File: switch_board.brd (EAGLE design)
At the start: 15 parts, among them U1 ADG904BRUZ, U2 ADP3330ARTZ-2.5-R7

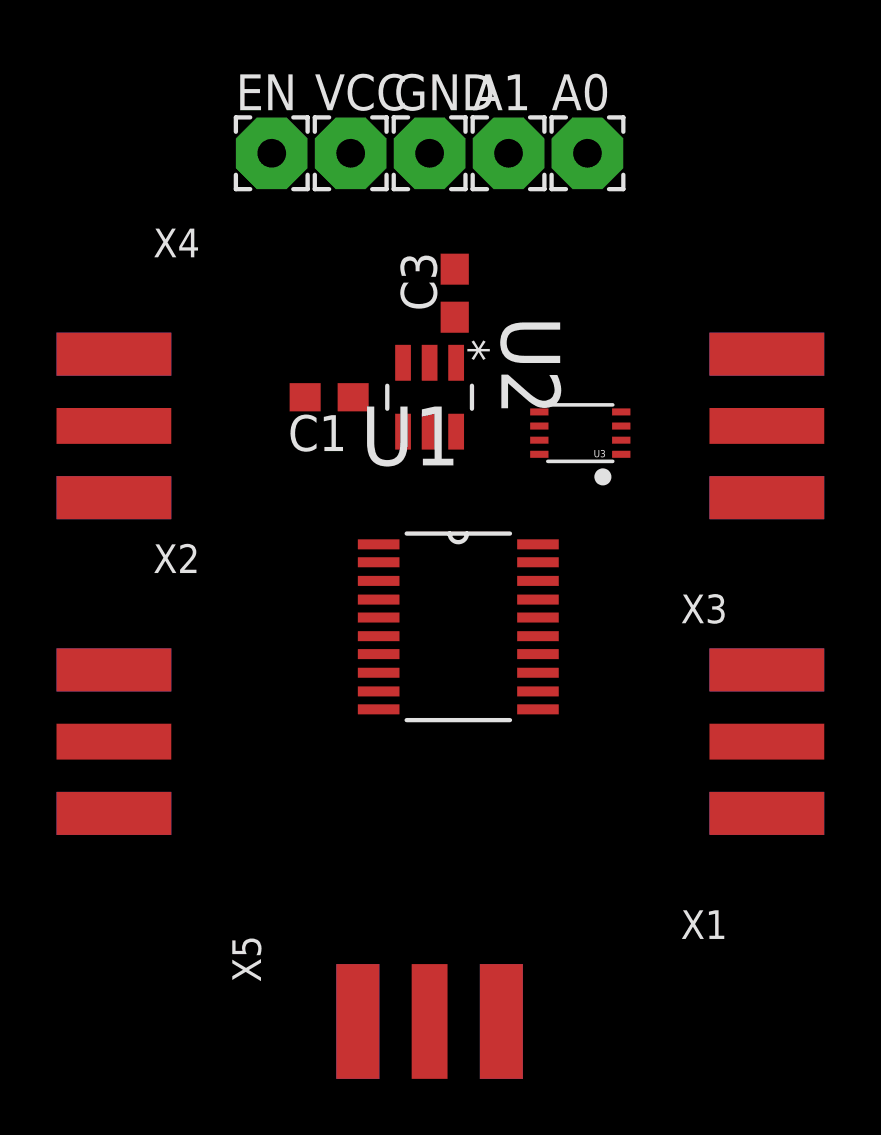
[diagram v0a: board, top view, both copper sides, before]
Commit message: Add DC Blocking Caps
Added 100uf caps for dc blocking on rf lines. Also updated readme
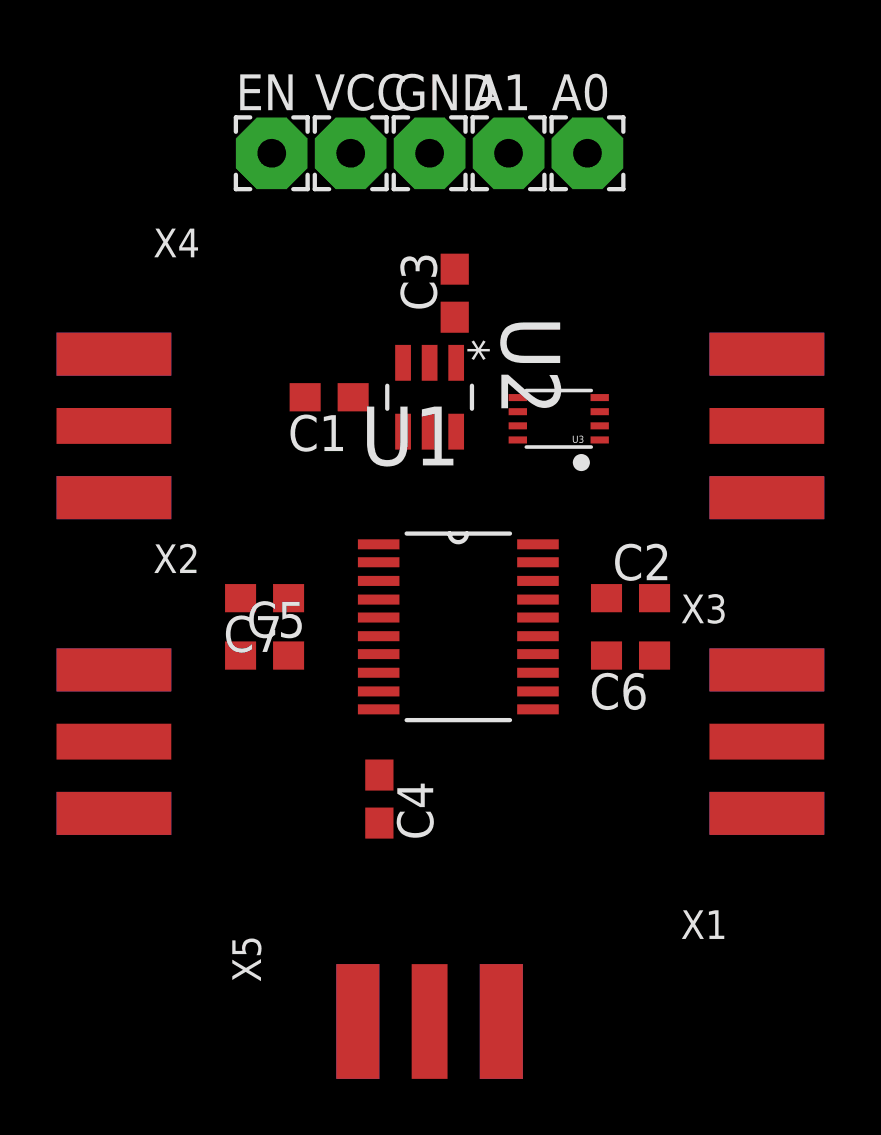
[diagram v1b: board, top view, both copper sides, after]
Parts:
- added C2, C4, C5, C6, C7: 0.1uF, resistor:C0603
- moved U3 0.92 mm to (17.8, 13.7)
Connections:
- removed net RF2: U1.17, X3.P
- new net N$3: C5.1, X2.P
- new net N$4: C4.1, U1.10
- new net N$5: C2.1, U1.17
- new net N$7: C2.2, X3.P
- new net N$8: C7.2, X4.P
- new net N$9: C6.1, X1.P
- net RF1: now also C7.1; no longer X4.P
- net RF3: now also C5.2; no longer X2.P
- net RF4: now also C6.2; no longer X1.P
- net RFC: now also C4.2; no longer U1.10
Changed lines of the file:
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@@
 <setting verticaltext="up"/>
 </settings>
-<grid distance="10" unitdist="mil" unit="mil" style="lines" multiple="1" display="no" altdistance="5" altunitdist="mil" altunit="mil"/>
+<grid distance="10" unitdist="mil" unit="mm" style="lines" multiple="1" display="yes" altdistance="5" altunitdist="mil" altunit="mil"/>
 <layers>
 <layer number="1" name="Top" color="4" fill="1" visible="yes" active="yes"/>
@@
 <element name="C1" library="resistor" library_urn="urn:adsk.eagle:library:348" package="C0603" value="0.47uF" x="9.652" y="14.478" rot="R180"/>
 <element name="C3" library="resistor" library_urn="urn:adsk.eagle:library:348" package="C0603" value="0.47uF" x="14.097" y="18.161" rot="R90"/>
-<element name="U3" library="adafruit" library_urn="urn:adsk.eagle:library:420" package="VFSOP-8" value="" x="18.542" y="13.208" rot="R90"/>
+<element name="U3" library="adafruit" library_urn="urn:adsk.eagle:library:420" package="VFSOP-8" value="" x="17.78" y="13.716" rot="R90"/>
+<element name="C2" library="resistor" library_urn="urn:adsk.eagle:library:348" package="C0603" value="0.1uF" x="20.32" y="7.366"/>
+<element name="C4" library="resistor" library_urn="urn:adsk.eagle:library:348" package="C0603" value="0.1uF" x="11.43" y="0.254" rot="R270"/>
+<element name="C5" library="resistor" library_urn="urn:adsk.eagle:library:348" package="C0603" value="0.1uF" x="7.366" y="5.334"/>
+<element name="C6" library="resistor" library_urn="urn:adsk.eagle:library:348" package="C0603" value="0.1uF" x="20.32" y="5.334" rot="R180"/>
+<element name="C7" library="resistor" library_urn="urn:adsk.eagle:library:348" package="C0603" value="0.1uF" x="7.366" y="7.366" rot="R180"/>
 </elements>
 <signals>
@@
 <contactref element="X4" pad="GND@4"/>
 <contactref element="X4" pad="GND@3"/>
-<contactref element="X3" pad="GND@4"/>
-<contactref element="X3" pad="GND@3"/>
 <contactref element="X3" pad="GND@2"/>
 <contactref element="X3" pad="GND@1"/>
@@
 <contactref element="X4" pad="GND@1"/>
 <contactref element="U3" pad="P$2"/>
+<contactref element="X3" pad="GND@4"/>
+<contactref element="X3" pad="GND@3"/>
 <wire x1="25.146" y1="16.002" x2="25.146" y2="16.002" width="0" layer="19" extent="1-16"/>
-<wire x1="25.146" y1="10.922" x2="25.146" y2="16.002" width="0" layer="19" extent="16-16"/>
+<wire x1="25.146" y1="10.922" x2="25.146" y2="16.002" width="0" layer="19" extent="1-1"/>
 <wire x1="25.146" y1="10.922" x2="25.146" y2="10.922" width="0" layer="19" extent="1-16"/>
-<wire x1="19.992" y1="12.958" x2="25.146" y2="10.922" width="0" layer="19" extent="1-16"/>
-<wire x1="17.0434" y1="7.9756" x2="19.992" y2="12.958" width="0" layer="19" extent="1-1"/>
+<wire x1="25.146" y1="4.826" x2="25.146" y2="10.922" width="0" layer="19" extent="1-16"/>
+<wire x1="25.146" y1="4.826" x2="25.146" y2="4.826" width="0" layer="19" extent="1-16"/>
+<wire x1="25.146" y1="-0.254" x2="25.146" y2="4.826" width="0" layer="19" extent="16-16"/>
+<wire x1="25.146" y1="-0.254" x2="25.146" y2="-0.254" width="0" layer="19" extent="1-16"/>
+<wire x1="19.23" y1="13.466" x2="25.146" y2="16.002" width="0" layer="19" extent="1-1"/>
+<wire x1="17.0434" y1="7.9756" x2="19.23" y2="13.466" width="0" layer="19" extent="1-1"/>
 <wire x1="17.0434" y1="6.6802" x2="17.0434" y2="7.9756" width="0" layer="19" extent="1-1"/>
 <wire x1="17.0434" y1="6.0198" x2="17.0434" y2="6.6802" width="0" layer="19" extent="1-1"/>
@@
 <wire x1="12.2682" y1="13.2588" x2="11.4046" y2="9.271" width="0" layer="19" extent="1-1"/>
 <wire x1="8.802" y1="14.478" x2="12.2682" y2="13.2588" width="0" layer="19" extent="1-1"/>
-<wire x1="25.146" y1="4.826" x2="25.146" y2="10.922" width="0" layer="19" extent="16-16"/>
-<wire x1="25.146" y1="4.826" x2="25.146" y2="4.826" width="0" layer="19" extent="1-16"/>
-<wire x1="25.146" y1="-0.254" x2="25.146" y2="4.826" width="0" layer="19" extent="16-16"/>
-<wire x1="25.146" y1="-0.254" x2="25.146" y2="-0.254" width="0" layer="19" extent="1-16"/>
 <wire x1="14.097" y1="19.011" x2="12.2682" y2="13.2588" width="0" layer="19" extent="1-1"/>
 <wire x1="13.208" y1="23.114" x2="14.097" y2="19.011" width="0" layer="19" extent="1-1"/>
@@
 <wire x1="13.208" y1="15.6972" x2="10.414" y2="23.114" width="0" layer="19" extent="1-1"/>
 <wire x1="10.502" y1="14.478" x2="13.208" y2="15.6972" width="0" layer="19" extent="1-1"/>
-<wire x1="17.092" y1="12.958" x2="13.208" y2="15.6972" width="0" layer="19" extent="1-1"/>
+<wire x1="16.33" y1="13.466" x2="13.208" y2="15.6972" width="0" layer="19" extent="1-1"/>
 </signal>
 <signal name="N$1">
@@
 <signal name="RF1">
 <contactref element="U1" pad="4"/>
-<contactref element="X4" pad="P"/>
-<wire x1="2.032" y1="13.462" x2="11.4046" y2="7.3152" width="0" layer="19" extent="1-1"/>
-</signal>
-<signal name="RF2">
-<contactref element="U1" pad="17"/>
-<contactref element="X3" pad="P"/>
-<wire x1="17.0434" y1="7.3152" x2="25.146" y2="13.462" width="0" layer="19" extent="1-1"/>
+<contactref element="C7" pad="1"/>
+<wire x1="8.216" y1="7.366" x2="11.4046" y2="7.3152" width="0" layer="19" extent="1-1"/>
 </signal>
 <signal name="RF3">
 <contactref element="U1" pad="7"/>
-<contactref element="X2" pad="P"/>
-<wire x1="2.032" y1="2.286" x2="11.4046" y2="5.3848" width="0" layer="19" extent="1-1"/>
+<contactref element="C5" pad="2"/>
+<wire x1="8.216" y1="5.334" x2="11.4046" y2="5.3848" width="0" layer="19" extent="1-1"/>
 </signal>
 <signal name="RF4">
-<contactref element="X1" pad="P"/>
 <contactref element="U1" pad="14"/>
-<wire x1="17.0434" y1="5.3848" x2="25.146" y2="2.286" width="0" layer="19" extent="1-1"/>
+<contactref element="C6" pad="2"/>
+<wire x1="19.47" y1="5.334" x2="17.0434" y2="5.3848" width="0" layer="19" extent="1-1"/>
 </signal>
 <signal name="RFC">
-<contactref element="U1" pad="10"/>
 <contactref element="X5" pad="P"/>
-<wire x1="13.208" y1="-7.62" x2="11.4046" y2="3.429" width="0" layer="19" extent="1-1"/>
+<contactref element="C4" pad="2"/>
+<wire x1="13.208" y1="-7.62" x2="11.43" y2="-0.596" width="0" layer="19" extent="1-1"/>
 </signal>
 <signal name="N$6">
@@
 <contactref element="C3" pad="1"/>
 <contactref element="U3" pad="P$3"/>
-<wire x1="14.1478" y1="15.6972" x2="19.992" y2="13.458" width="0" layer="19" extent="1-1"/>
+<wire x1="14.1478" y1="15.6972" x2="19.23" y2="13.966" width="0" layer="19" extent="1-1"/>
 <wire x1="14.097" y1="17.311" x2="14.1478" y2="15.6972" width="0" layer="19" extent="1-1"/>
 <wire x1="11.4046" y1="8.636" x2="14.1478" y2="15.6972" width="0" layer="19" extent="1-1"/>
@@
 <contactref element="A0" pad="1"/>
 <contactref element="U3" pad="P$8"/>
-<wire x1="17.092" y1="12.458" x2="18.796" y2="23.114" width="0" layer="19" extent="1-1"/>
+<wire x1="16.33" y1="12.966" x2="18.796" y2="23.114" width="0" layer="19" extent="1-1"/>
 </signal>
 <signal name="A1_TTL">
 <contactref element="A1" pad="1"/>
 <contactref element="U3" pad="P$1"/>
-<wire x1="19.992" y1="12.458" x2="16.002" y2="23.114" width="0" layer="19" extent="1-1"/>
+<wire x1="19.23" y1="12.966" x2="16.002" y2="23.114" width="0" layer="19" extent="1-1"/>
 </signal>
 <signal name="A1_LVTTL">
 <contactref element="U3" pad="P$4"/>
 <contactref element="U1" pad="19"/>
-<wire x1="17.0434" y1="8.636" x2="19.992" y2="13.958" width="0" layer="19" extent="1-1"/>
+<wire x1="17.0434" y1="8.636" x2="19.23" y2="14.466" width="0" layer="19" extent="1-1"/>
 </signal>
 <signal name="A0_LVTTL">
 <contactref element="U3" pad="P$5"/>
 <contactref element="U1" pad="20"/>
-<wire x1="17.0434" y1="9.271" x2="17.092" y2="13.958" width="0" layer="19" extent="1-1"/>
+<wire x1="17.0434" y1="9.271" x2="16.33" y2="14.466" width="0" layer="19" extent="1-1"/>
+</signal>
+<signal name="N$3">
+<contactref element="X2" pad="P"/>
+<contactref element="C5" pad="1"/>
+<wire x1="2.032" y1="2.286" x2="6.516" y2="5.334" width="0" layer="19" extent="1-1"/>
+</signal>
+<signal name="N$4">
+<contactref element="U1" pad="10"/>
+<contactref element="C4" pad="1"/>
+<wire x1="11.43" y1="1.104" x2="11.4046" y2="3.429" width="0" layer="19" extent="1-1"/>
+</signal>
+<signal name="N$5">
+<contactref element="U1" pad="17"/>
+<contactref element="C2" pad="1"/>
+<wire x1="17.0434" y1="7.3152" x2="19.47" y2="7.366" width="0" layer="19" extent="1-1"/>
+</signal>
+<signal name="N$7">
+<contactref element="C2" pad="2"/>
+<contactref element="X3" pad="P"/>
+<wire x1="21.17" y1="7.366" x2="25.146" y2="13.462" width="0" layer="19" extent="1-1"/>
+</signal>
+<signal name="N$8">
+<contactref element="C7" pad="2"/>
+<contactref element="X4" pad="P"/>
+<wire x1="2.032" y1="13.462" x2="6.516" y2="7.366" width="0" layer="19" extent="1-1"/>
+</signal>
+<signal name="N$9">
+<contactref element="C6" pad="1"/>
+<contactref element="X1" pad="P"/>
+<wire x1="21.17" y1="5.334" x2="25.146" y2="2.286" width="0" layer="19" extent="1-1"/>
 </signal>
 </signals>
